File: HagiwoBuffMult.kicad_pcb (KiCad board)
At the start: 2 copper layers, 25.4 x 108.3 mm, 43 parts, among them J10 Conn_01x01_Pin, J11 Conn_01x01_Pin, J12 Conn_01x01_Pin, J13 Conn_01x01_Pin, J14 Conn_01x01_Pin, J15 Conn_01x01_Pin, J16 Conn_01x01_Pin, J17 Conn_01x01_Socket, J18 Conn_01x01_Socket, J19 Conn_01x01_Socket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

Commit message: routed and made panel
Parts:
- removed C3, C4: 100n, Capacitor_THT:C_Axial_L3.8mm_D2.6mm_P7.50mm_Horizontal
- removed IN1, IN2, OUT1, OUT2, OUT3, OUT4, OUT5, OUT6: 3.5mm_Mono_Switched_sm, Library:EighthInch_PJ398SM_3mmNPTH
- added J1: IN1, Library:EighthInch_PJ398SM_3mmNPTH, F.Cu at (106.7, 57.5)
- added J2: IN2, Library:EighthInch_PJ398SM_3mmNPTH, F.Cu at (106.7, 111.4)
- added J4: OUT1, Library:EighthInch_PJ398SM_3mmNPTH, F.Cu at (106.7, 71.0)
- added J5: OUT2, Library:EighthInch_PJ398SM_3mmNPTH, F.Cu at (106.7, 84.5)
- added J6: OUT3, Library:EighthInch_PJ398SM_3mmNPTH, F.Cu at (106.7, 97.9)
- added J7: OUT4, Library:EighthInch_PJ398SM_3mmNPTH, F.Cu at (106.7, 124.8)
- added J8: OUT5, Library:EighthInch_PJ398SM_3mmNPTH, F.Cu at (106.7, 138.3)
- added J9: OUT6, Library:EighthInch_PJ398SM_3mmNPTH, F.Cu at (106.7, 151.8)
- added REF**: GND, PCM_4ms_Faceplate:Faceplate_Hole_Jack_3.5mm, F.Cu at (91.4, 138.3)
- added REF**: GND, PCM_4ms_Faceplate:Faceplate_Hole_Jack_3.5mm, F.Cu at (91.4, 57.5)
- added REF**: GND, PCM_4ms_Faceplate:Faceplate_Hole_Jack_3.5mm, F.Cu at (91.4, 97.9)
- added REF**: GND, PCM_4ms_Faceplate:Faceplate_Hole_Jack_3.5mm, F.Cu at (91.4, 111.4)
- added REF**: GND, PCM_4ms_Faceplate:Faceplate_Hole_Jack_3.5mm, F.Cu at (91.4, 151.8)
- added REF**: GND, PCM_4ms_Faceplate:Faceplate_Hole_Jack_3.5mm, F.Cu at (91.4, 84.5)
- added REF**: GND, PCM_4ms_Faceplate:Faceplate_Hole_Jack_3.5mm, F.Cu at (91.4, 124.8)
- added REF**: GND, PCM_4ms_Faceplate:Faceplate_Hole_Jack_3.5mm, F.Cu at (91.4, 71.0)
- J10: renamed from J17; value Conn_01x01_Socket -> S
- J11: renamed from J18; value Conn_01x01_Socket -> S
- J12: renamed from J19; value Conn_01x01_Socket -> S
- J13: renamed from J20; value Conn_01x01_Socket -> S
- J14: renamed from J21; value Conn_01x01_Socket -> S
- J15: renamed from J22; value Conn_01x01_Socket -> S
- J16: renamed from J23; value Conn_01x01_Socket -> S
- J17: renamed from J24; value Conn_01x01_Socket -> S
- J18: renamed from J25; value Conn_01x01_Socket -> S
- J19: renamed from J26; value Conn_01x01_Socket -> S
- J20: renamed from J6; value Conn_01x01_Pin -> P
- J21: renamed from J7; value Conn_01x01_Pin -> P
- J22: renamed from J8; value Conn_01x01_Pin -> P
- J23: renamed from J10; value Conn_01x01_Pin -> P
- J24: renamed from J11; value Conn_01x01_Pin -> P
- J25: renamed from J12; value Conn_01x01_Pin -> P
- J26: renamed from J13; value Conn_01x01_Pin -> P
- J27: renamed from J14; value Conn_01x01_Pin -> P
- J28: renamed from J15; value Conn_01x01_Pin -> P
- J29: renamed from J16; value Conn_01x01_Pin -> P
- moved J21 0.28 mm to (125.2, 130.6)
- moved J22 0.25 mm to (118.7, 117.1)
- moved J26 0.25 mm to (125.1, 117.1)
- moved J27 0.25 mm to (118.7, 130.6)
- moved J12 0.13 mm to (103.5, 117.1)
- moved J16 0.13 mm to (109.9, 117.1)
- moved J17 0.13 mm to (103.5, 130.6)
- moved J10 0.13 mm to (103.5, 76.8)
- moved J11 0.13 mm to (110.0, 130.6)
- renumbered J9 to J3, R5 to R2, R2 to R3, R3 to R4, R4 to R5
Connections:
- U2 pad 3: IN1_PIN1_C -> IN2_PIN1_C
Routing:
- net IN2_PIN1_C: track 0.00 -> 73.6 mm, vias 0 -> 4
- net IN1_PIN1_C: track 108.0 -> 75.6 mm, vias 6 -> 1
- net OUT4_PIN1_C: track 60.2 -> 42.0 mm
- net -12V: track 90.2 -> 86.1 mm, vias 3 -> 0
- net IN2_PIN1_S: track 26.5 -> 30.1 mm
- net Net-(U2C--): track 15.2 -> 18.6 mm
- net OUT1_PIN1_C: track 83.0 -> 86.2 mm, vias 0 -> 6
- net OUT2_PIN1_C: track 69.1 -> 66.4 mm, vias 3 -> 7
- net GND_S: track 2.63 -> 0.00 mm
- net OUT5_PIN1_C: track 50.9 -> 53.4 mm, vias 4 -> 8
- net IN2_PIN3_C: track 37.8 -> 39.5 mm
- net OUT6_PIN1_C: track 109.7 -> 111.4 mm, vias 8 -> 10
- net OUT3_PIN1_C: track 33.2 -> 34.7 mm, vias 0 -> 5
- net +12V: track 81.6 -> 83.1 mm, vias 1 -> 0
- net Net-(U2B-+): track 25.3 -> 26.5 mm
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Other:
- board size 25.4 x 108.3 mm -> 40.6 x 128.5 mm
- board text added: "BUFF MULT"
- board text removed: "Cut holes in jack centres?"

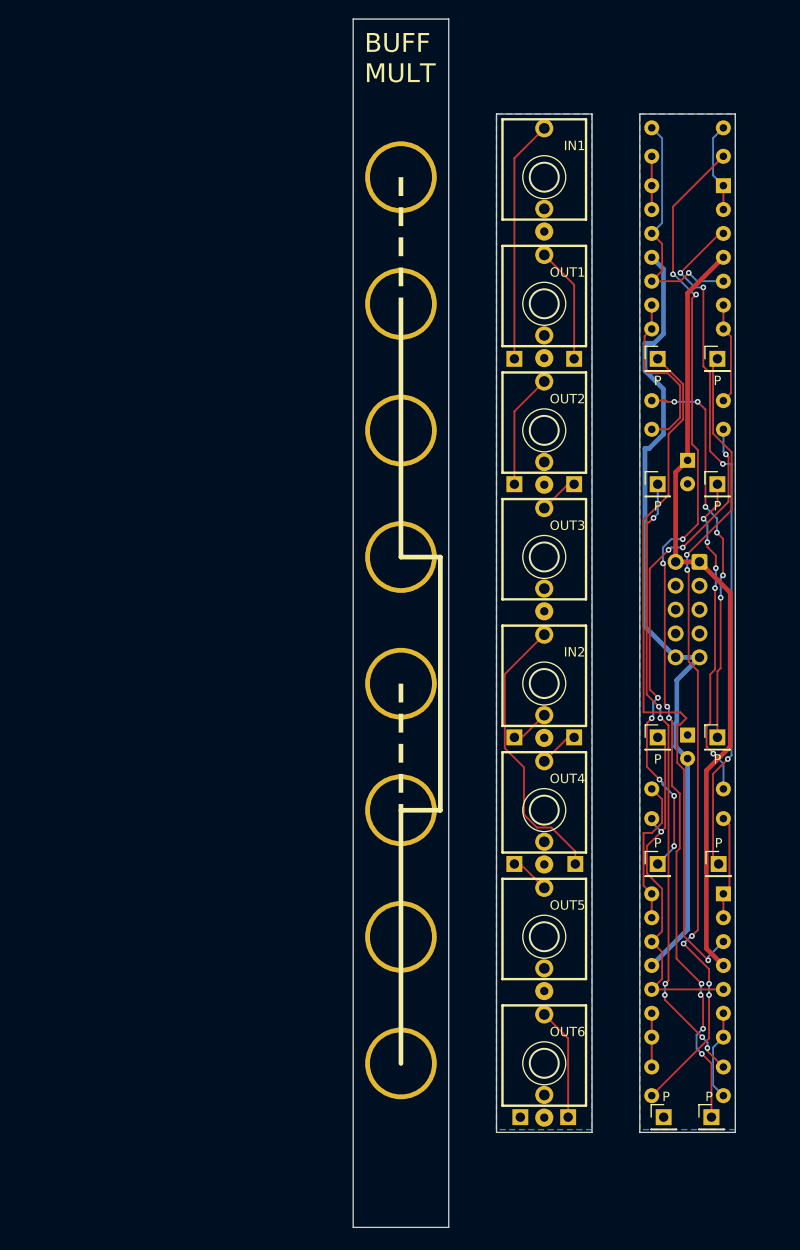
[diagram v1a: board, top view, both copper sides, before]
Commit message: broke panel out into separate file and made board and panel width narrower in accordance with doefper A100 standard
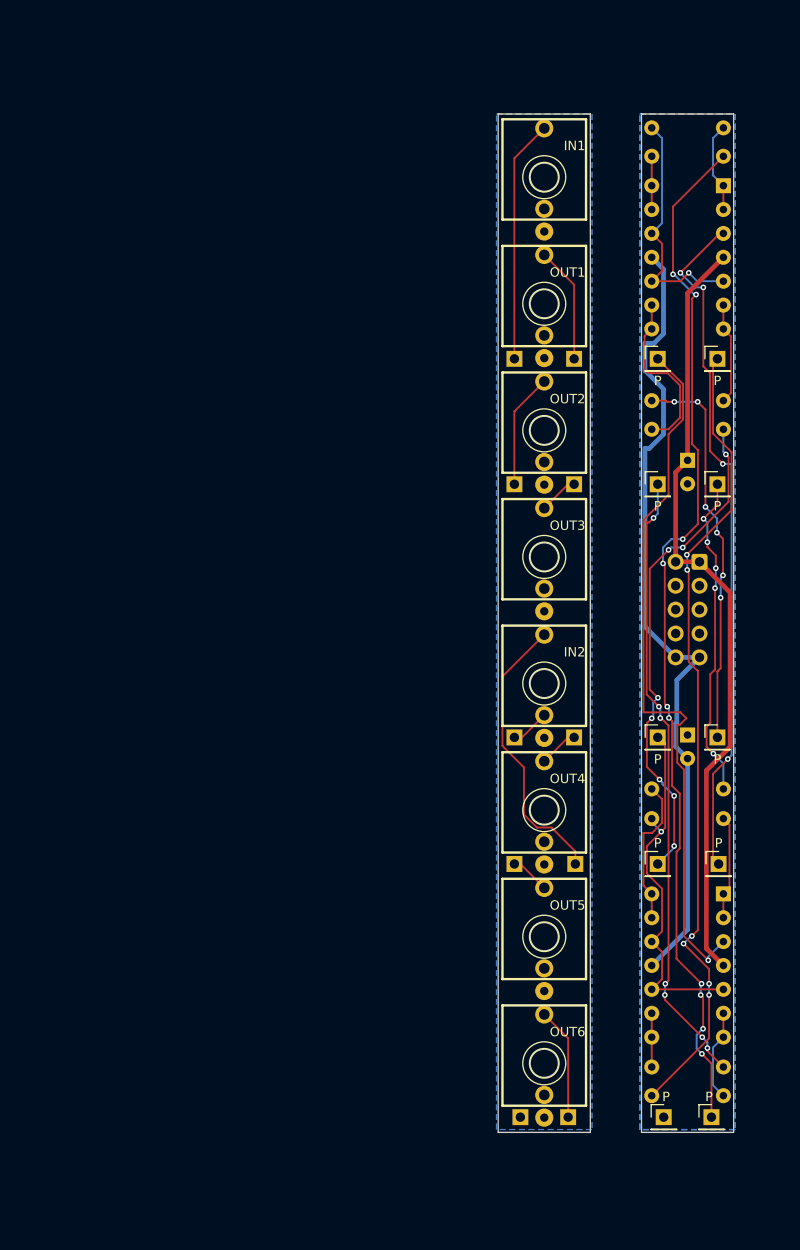
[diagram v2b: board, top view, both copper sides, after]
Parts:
- removed REF** (x8): GND, PCM_4ms_Faceplate:Faceplate_Hole_Jack_3.5mm
- J3: footprint Library:IDC-Header_2x05_P2.54mm_Vertical_Euro_Power_Striped -> Library:IDC-Header_2x05_P2.54mm_Vertical_Euro_Power_Striped_ThickerText
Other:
- board size 40.6 x 128.5 mm -> 25 x 108.3 mm
- board text removed: "BUFF MULT"

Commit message: added branding and instructions
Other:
- board text added: "BOARD 1/2"
- board text added: "BOARD 2/2"
- board text added: "BOTTOM"
- board text added: "HAGIWO BUFF MULT"
- board text added: "JLCJLCJLCJLC"
- board text added: "PCB BY 42 BERLIN SYNTHLAB"
- board text added: "TOP"
- board text added: "V1.0"

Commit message: v1.0 ready for production
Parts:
- C1, C2: value 10u -> 10uF; footprint Capacitor_THT:CP_Radial_D5.0mm_P2.50mm -> Capacitor_THT:CP_Radial_D4.0mm_P1.50mm
- J10, J11, J12, J13, J14, J15, J16, J17, J18, J19: value S -> Conn_01x01_Socket
- J20, J21, J22, J23, J24, J25, J26, J27, J28, J29: value P -> Conn_01x01_Pin
- moved J20 50.8 mm to (67.9, 76.8)
- moved J22 50.8 mm to (67.9, 117.1)
- moved J24 50.8 mm to (67.9, 90.2)
- moved J27 50.8 mm to (67.9, 130.6)
- moved J1 50.8 mm to (55.9, 57.5)
- moved J13 50.8 mm to (59.1, 76.8)
- moved J15 50.8 mm to (59.1, 90.2)
- moved J16 50.8 mm to (59.1, 117.1)
- moved J2 50.8 mm to (55.9, 111.4)
- moved J4 50.8 mm to (55.9, 71.0)
- moved J5 50.8 mm to (55.9, 84.5)
- moved J6 50.8 mm to (55.9, 97.9)
- moved J7 50.8 mm to (55.9, 124.8)
- moved J8 50.8 mm to (55.9, 138.3)
- moved J9 50.8 mm to (55.9, 151.8)
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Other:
- board text added: "1/2 BOTTOM"
- board text added: "2/2 BOTTOM"
- board text added: "P = PIN S = SOCKET"
- board text added: "SynthLab"
- board text added: "github.com/fablabnk/SynthLabProjects"
- board text removed: "BOARD 1/2"
- board text removed: "BOARD 2/2"
- board text removed: "BOTTOM"
